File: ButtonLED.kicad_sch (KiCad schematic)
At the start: 20 parts

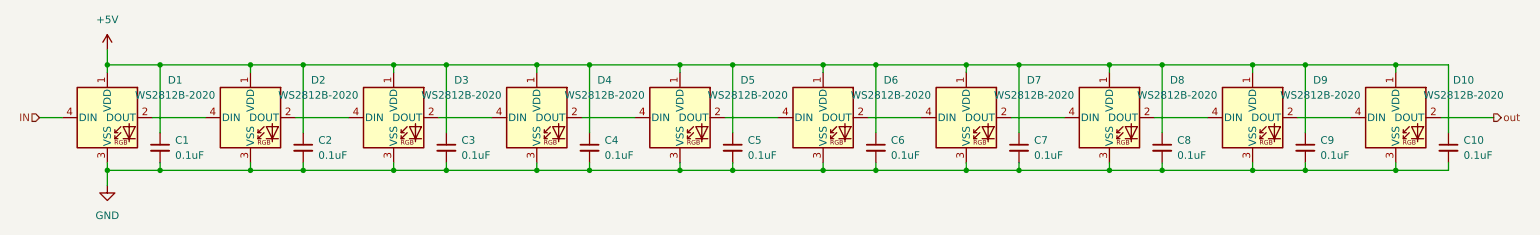
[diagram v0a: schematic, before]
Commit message: 外周LEDを116個に修正
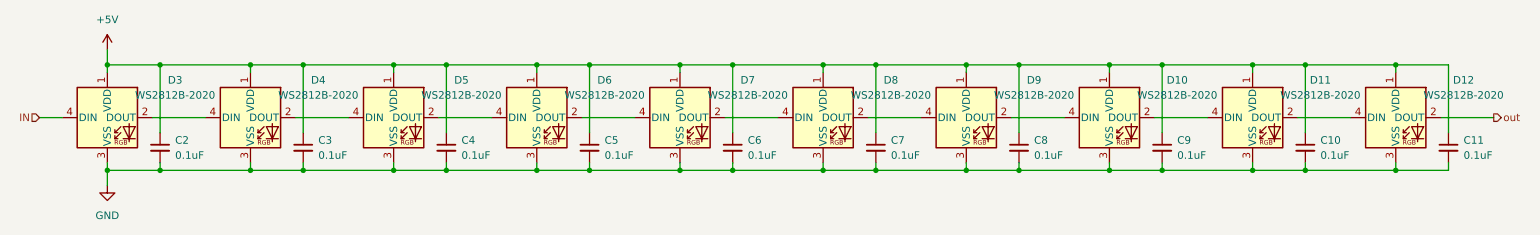
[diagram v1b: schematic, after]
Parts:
- renumbered C9 to C10, C10 to C11, C1 to C2, C2 to C3, C3 to C4, C4 to C5, C5 to C6, C6 to C7, C7 to C8, C8 to C9, D8 to D10, D9 to D11, D10 to D12, D1 to D3, D2 to D4, D3 to D5, D4 to D6, D5 to D7, D6 to D8, D7 to D9
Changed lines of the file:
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@@
 		(dnp no)
 		(fields_autoplaced yes)
-		(property "Reference" "D4"
+		(property "Reference" "D6"
 			(at 123.19 90.2014 0)
 			(effects
@@
 		(dnp no)
 		(fields_autoplaced yes)
-		(property "Reference" "D9"
+		(property "Reference" "D11"
 			(at 243.84 90.2014 0)
 			(effects
@@
 		(dnp no)
 		(fields_autoplaced yes)
-		(property "Reference" "D10"
+		(property "Reference" "D12"
 			(at 267.97 90.2014 0)
 			(effects
@@
 		(dnp no)
 		(fields_autoplaced yes)
-		(property "Reference" "D3"
+		(property "Reference" "D5"
 			(at 99.06 90.2014 0)
 			(effects
@@
 		(dnp no)
 		(fields_autoplaced yes)
-		(property "Reference" "C3"
+		(property "Reference" "C4"
 			(at 99.06 100.3362 0)
 			(effects
@@
 		(dnp no)
 		(fields_autoplaced yes)
-		(property "Reference" "C2"
+		(property "Reference" "C3"
 			(at 74.93 100.3362 0)
 			(effects
@@
 		(dnp no)
 		(fields_autoplaced yes)
-		(property "Reference" "D8"
+		(property "Reference" "D10"
 			(at 219.71 90.2014 0)
 			(effects
@@
 		(dnp no)
 		(fields_autoplaced yes)
-		(property "Reference" "C8"
+		(property "Reference" "C9"
 			(at 219.71 100.3362 0)
 			(effects
@@
 		(dnp no)
 		(fields_autoplaced yes)
-		(property "Reference" "D2"
+		(property "Reference" "D4"
 			(at 74.93 90.2014 0)
 			(effects
@@
 		(dnp no)
 		(fields_autoplaced yes)
-		(property "Reference" "C5"
+		(property "Reference" "C6"
 			(at 147.32 100.3362 0)
 			(effects
@@
 		(dnp no)
 		(fields_autoplaced yes)
-		(property "Reference" "C9"
+		(property "Reference" "C10"
 			(at 243.84 100.3362 0)
 			(effects
@@
 		(dnp no)
 		(fields_autoplaced yes)
-		(property "Reference" "C1"
+		(property "Reference" "C2"
 			(at 50.8 100.3362 0)
 			(effects
@@
 		(dnp no)
 		(fields_autoplaced yes)
-		(property "Reference" "D1"
+		(property "Reference" "D3"
 			(at 50.8 90.2014 0)
 			(effects
@@
 		(dnp no)
 		(fields_autoplaced yes)
-		(property "Reference" "C4"
+		(property "Reference" "C5"
 			(at 123.19 100.3362 0)
 			(effects
@@
 		(dnp no)
 		(fields_autoplaced yes)
-		(property "Reference" "C10"
+		(property "Reference" "C11"
 			(at 267.97 100.3362 0)
 			(effects
@@
 		(dnp no)
 		(fields_autoplaced yes)
-		(property "Reference" "#PWR02"
+		(property "Reference" "#PWR012"
 			(at 39.37 114.3 0)
 			(effects
@@
 		(dnp no)
 		(fields_autoplaced yes)
-		(property "Reference" "#PWR01"
+		(property "Reference" "#PWR011"
 			(at 39.37 88.9 0)
 			(effects
@@
 		(dnp no)
 		(fields_autoplaced yes)
-		(property "Reference" "C7"
+		(property "Reference" "C8"
 			(at 195.58 100.3362 0)
 			(effects
@@
 		(dnp no)
 		(fields_autoplaced yes)
-		(property "Reference" "D7"
+		(property "Reference" "D9"
 			(at 195.58 90.2014 0)
 			(effects
@@
 		(dnp no)
 		(fields_autoplaced yes)
-		(property "Reference" "C6"
+		(property "Reference" "C7"
 			(at 171.45 100.3362 0)
 			(effects
@@
 		(dnp no)
 		(fields_autoplaced yes)
-		(property "Reference" "D6"
+		(property "Reference" "D8"
 			(at 171.45 90.2014 0)
 			(effects
@@
 		(dnp no)
 		(fields_autoplaced yes)
-		(property "Reference" "D5"
+		(property "Reference" "D7"
 			(at 147.32 90.2014 0)
 			(effects

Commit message: 部品修正
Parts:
- D10, D11, D12, D3, D4, D5, D6, D7, D8, D9: footprint LED_SMD:LED_WS2812B_PLCC4_5.0x5.0mm_P3.2mm -> LED_SMD:LED_WS2812B-2020_PLCC4_2.0x2.0mm; symbol LED:WS2812B -> LED:WS2812B-2020
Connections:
- net +5V: now also D10.4 (VDD), D11.4 (VDD), D12.4 (VDD), D3.4 (VDD), D4.4 (VDD), D5.4 (VDD), D6.4 (VDD), D7.4 (VDD), D8.4 (VDD), D9.4 (VDD); no longer D10.1 (VDD), D11.1 (VDD), D12.1 (VDD), D3.1 (VDD), D4.1 (VDD), D5.1 (VDD), D6.1 (VDD), D7.1 (VDD), D8.1 (VDD), D9.1 (VDD)
- net GND: now also D10.2 (VSS), D11.2 (VSS), D12.2 (VSS), D3.2 (VSS), D4.2 (VSS), D5.2 (VSS), D6.2 (VSS), D7.2 (VSS), D8.2 (VSS), D9.2 (VSS); no longer D10.3 (VSS), D11.3 (VSS), D12.3 (VSS), D3.3 (VSS), D4.3 (VSS), D5.3 (VSS), D6.3 (VSS), D7.3 (VSS), D8.3 (VSS), D9.3 (VSS)
- net IN: now also D3.3 (DIN); no longer D3.4 (DIN)
- net out: now also D12.1 (DOUT); no longer D12.2 (DOUT)
- new net: D6.1 (DOUT), D7.3 (DIN)
- new net: D5.1 (DOUT), D6.3 (DIN)
- new net: D11.1 (DOUT), D12.3 (DIN)
- new net: D10.1 (DOUT), D11.3 (DIN)
- new net: D4.1 (DOUT), D5.3 (DIN)
- new net: D10.3 (DIN), D9.1 (DOUT)
- new net: D3.1 (DOUT), D4.3 (DIN)
- new net: D8.1 (DOUT), D9.3 (DIN)
- new net: D7.1 (DOUT), D8.3 (DIN)
